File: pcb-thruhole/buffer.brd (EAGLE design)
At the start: 98 x 24 mm, 16 parts, among them IC1 LF353N, IC2 LF353N, IC3 LF353N

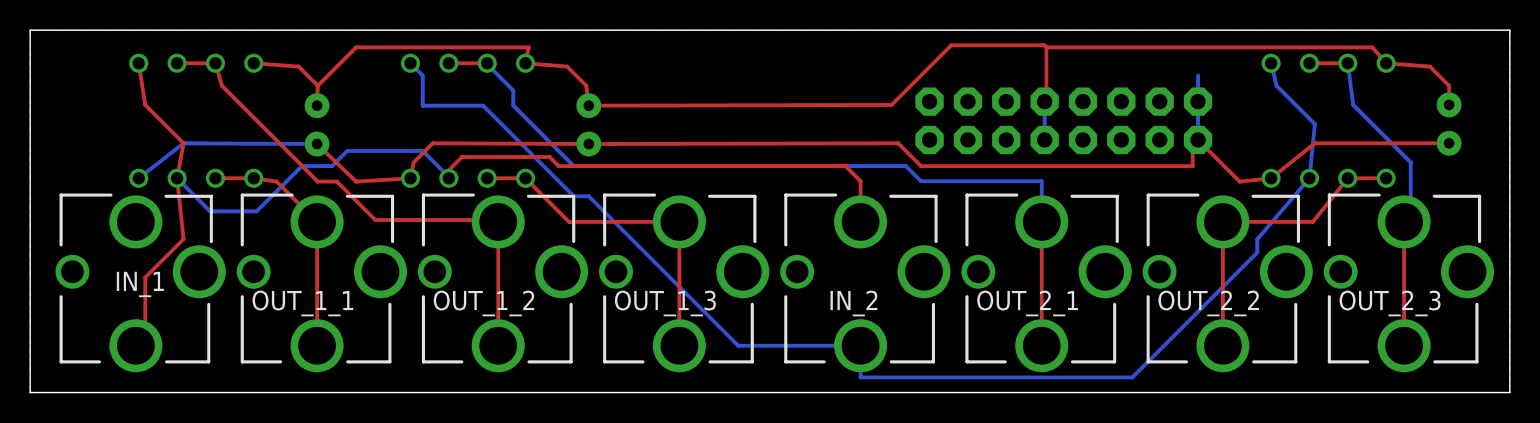
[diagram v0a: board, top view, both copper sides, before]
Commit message: straightened som traces.
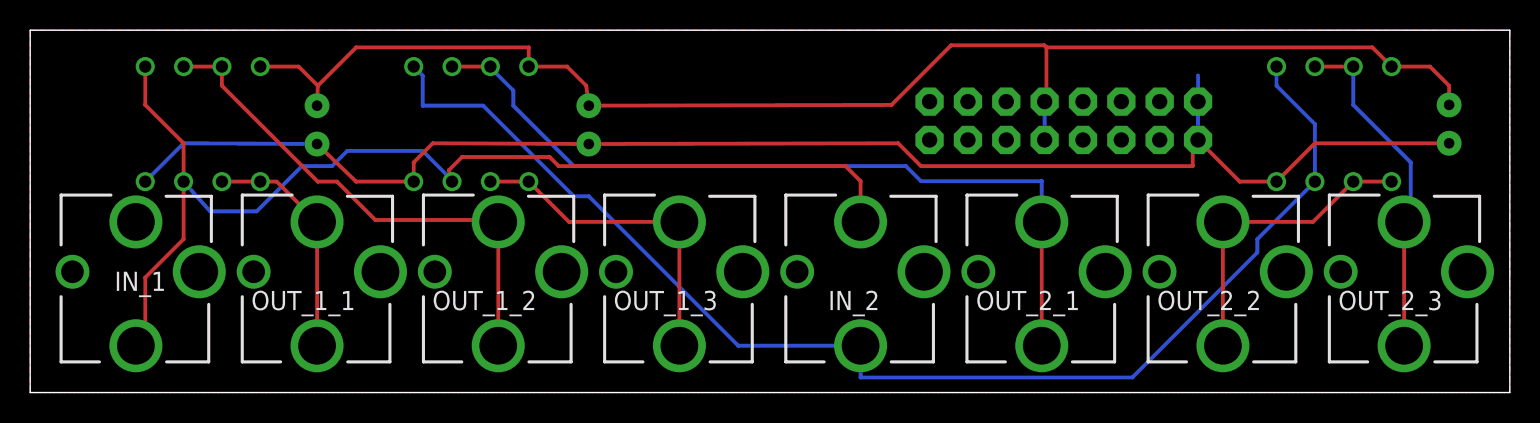
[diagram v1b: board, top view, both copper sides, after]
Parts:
- moved IC1 0.48 mm to (11.4, 17.8)
- moved IC3 0.42 mm to (86.4, 17.8)
- moved IC2 0.30 mm to (29.2, 17.8)
